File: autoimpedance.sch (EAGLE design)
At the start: 43 parts, among them IC1 AD5933, IC2 LM234, IC3 AD5245, Q1 DMG2307L-7

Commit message: Remove built for imp logo'
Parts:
- removed JP8: FIDUCIALUFIDUCIAL, SparkFun:FIDUCIALUFIDUCIAL
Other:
- note removed: "Electric Imp (based on their April design)"
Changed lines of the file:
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@@
 <part name="JP1" library="SparkFun-Connectors" deviceset="M02" device="SMD"/>
 <part name="U$5" library="SparkFun-Aesthetics" deviceset="OSHW-LOGO" device="S"/>
-<part name="JP8" library="SparkFun" deviceset="FIDUCIAL" device="UFIDUCIAL"/>
 <part name="OMNETICS" library="RHD2000" deviceset="OMNETICS_A79025" device=""/>
 <part name="IC1" library="autoimpedance" deviceset="AD5933" device=""/>
@@
 <text x="109.22" y="154.94" size="1.778" layer="97" rot="R90">1.5A</text>
 <text x="111.76" y="154.94" size="1.778" layer="97" rot="R90">VLF3014AT-2R2M1R2</text>
-<text x="150.622" y="6.35" size="3.048" layer="94">Electric Imp (based on their April design)</text>
 </plain>
 <instances>
@@
 <instance part="JP1" gate="G$1" x="10.16" y="119.38"/>
 <instance part="U$5" gate="G$1" x="132.08" y="10.16"/>
-<instance part="JP8" gate="G$1" x="243.84" y="33.02"/>
 <instance part="OMNETICS" gate="A" x="121.92" y="106.68" rot="R270"/>
 <instance part="IC1" gate="G$1" x="167.64" y="157.48"/>

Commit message: Fix incorrect VEE connection on 3x2 MUX
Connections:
- net 3.3V: no longer MUX3X2.VEE
- net GND: now also MUX3X2.VEE
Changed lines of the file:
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@@
 <part name="MUX3X2" library="open-ephys" deviceset="BU4053BC" device=""/>
 <part name="GND27" library="SparkFun-Aesthetics" deviceset="GND" device=""/>
-<part name="P+20" library="SparkFun-Aesthetics" deviceset="3.3V" device=""/>
 <part name="P+22" library="SparkFun-Aesthetics" deviceset="3.3V" device=""/>
 <part name="GND31" library="SparkFun-Aesthetics" deviceset="GND" device=""/>
@@
 <instance part="MUX3X2" gate="G$1" x="40.64" y="83.82"/>
 <instance part="GND27" gate="1" x="22.86" y="66.04"/>
-<instance part="P+20" gate="G$1" x="17.78" y="78.74"/>
 <instance part="P+22" gate="G$1" x="58.42" y="96.52"/>
 <instance part="GND31" gate="1" x="101.6" y="78.74"/>
@@
 <wire x1="30.48" y1="73.66" x2="22.86" y2="73.66" width="0.1524" layer="91"/>
 <wire x1="22.86" y1="73.66" x2="22.86" y2="68.58" width="0.1524" layer="91"/>
-<wire x1="22.86" y1="78.74" x2="22.86" y2="73.66" width="0.1524" layer="91"/>
+<wire x1="22.86" y1="78.74" x2="22.86" y2="76.2" width="0.1524" layer="91"/>
 <junction x="22.86" y="73.66"/>
 <pinref part="GND27" gate="1" pin="GND"/>
+<pinref part="MUX3X2" gate="G$1" pin="VEE"/>
+<wire x1="22.86" y1="76.2" x2="22.86" y2="73.66" width="0.1524" layer="91"/>
+<wire x1="30.48" y1="76.2" x2="22.86" y2="76.2" width="0.1524" layer="91"/>
+<junction x="22.86" y="76.2"/>
 </segment>
 <segment>
@@
 </segment>
 <segment>
-<pinref part="MUX3X2" gate="G$1" pin="VEE"/>
-<wire x1="30.48" y1="76.2" x2="17.78" y2="76.2" width="0.1524" layer="91"/>
-<wire x1="17.78" y1="76.2" x2="17.78" y2="78.74" width="0.1524" layer="91"/>
-<pinref part="P+20" gate="G$1" pin="3.3V"/>
-</segment>
-<segment>

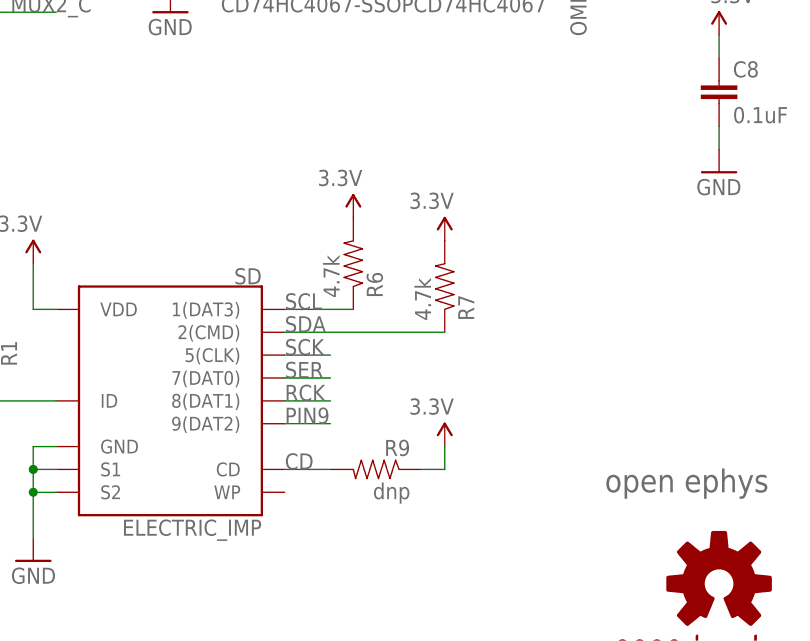
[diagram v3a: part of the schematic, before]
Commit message: Switch to i2c89 instead of i2c12
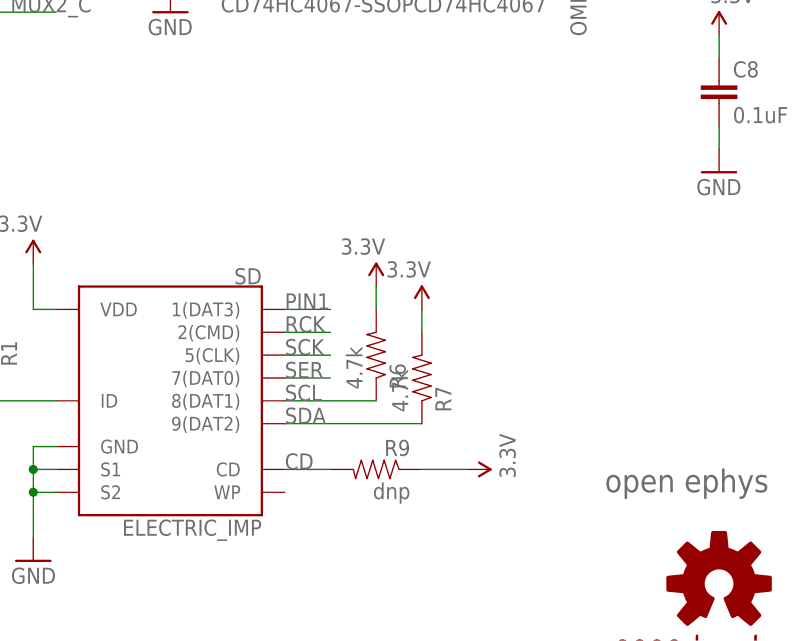
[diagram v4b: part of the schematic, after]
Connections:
- removed net PIN9: SD.9(DAT2)
- new net PIN1: SD.1(DAT3)
- net RCK: now also SD.2(CMD); no longer SD.8(DAT1)
- net SCL: now also SD.8(DAT1); no longer SD.1(DAT3)
- net SDA: now also SD.9(DAT2); no longer SD.2(CMD)
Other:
- moved on the sheet: R6, R7
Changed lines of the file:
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@@
 <instance part="GND13" gate="1" x="71.12" y="162.56"/>
 <instance part="GND14" gate="1" x="76.2" y="160.02"/>
-<instance part="R6" gate="G$1" x="91.44" y="45.72" rot="MR90"/>
-<instance part="R7" gate="G$1" x="101.6" y="43.18" rot="MR90"/>
-<instance part="P+6" gate="G$1" x="91.44" y="50.8" rot="MR0"/>
-<instance part="P+7" gate="G$1" x="101.6" y="48.26" rot="MR0"/>
+<instance part="R6" gate="G$1" x="93.98" y="35.56" rot="MR90"/>
+<instance part="R7" gate="G$1" x="99.06" y="33.02" rot="MR90"/>
+<instance part="P+6" gate="G$1" x="93.98" y="43.18" rot="MR0"/>
+<instance part="P+7" gate="G$1" x="99.06" y="40.64" rot="MR0"/>
 <instance part="P+8" gate="G$1" x="187.96" y="144.78" rot="R180"/>
 <instance part="GND15" gate="1" x="193.04" y="152.4"/>
@@
 <instance part="P+12" gate="G$1" x="238.76" y="162.56" rot="R270"/>
 <instance part="R9" gate="G$1" x="93.98" y="22.86" rot="MR0"/>
-<instance part="P+13" gate="G$1" x="101.6" y="25.4" rot="MR0"/>
+<instance part="P+13" gate="G$1" x="104.14" y="22.86" rot="MR90"/>
 <instance part="GND8" gate="1" x="152.4" y="53.34" rot="MR0"/>
 <instance part="GND20" gate="1" x="182.88" y="68.58" rot="MR270"/>
@@
 <pinref part="R6" gate="G$1" pin="2"/>
 <pinref part="P+6" gate="G$1" pin="3.3V"/>
+<wire x1="93.98" y1="40.64" x2="93.98" y2="43.18" width="0.1524" layer="91"/>
 </segment>
 <segment>
 <pinref part="R7" gate="G$1" pin="2"/>
 <pinref part="P+7" gate="G$1" pin="3.3V"/>
+<wire x1="99.06" y1="38.1" x2="99.06" y2="40.64" width="0.1524" layer="91"/>
 </segment>
 <segment>
@@
 <segment>
 <pinref part="R9" gate="G$1" pin="1"/>
-<wire x1="99.06" y1="22.86" x2="101.6" y2="22.86" width="0.1524" layer="91"/>
 <pinref part="P+13" gate="G$1" pin="3.3V"/>
-<wire x1="101.6" y1="22.86" x2="101.6" y2="25.4" width="0.1524" layer="91"/>
+<wire x1="99.06" y1="22.86" x2="104.14" y2="22.86" width="0.1524" layer="91"/>
 </segment>
 <segment>
@@
 </segment>
 </net>
-<net name="PIN9" class="0">
-<segment>
-<pinref part="SD" gate="G$1" pin="9(DAT2)"/>
-<wire x1="83.82" y1="27.94" x2="88.9" y2="27.94" width="0.1524" layer="91"/>
-<label x="83.82" y="27.94" size="1.778" layer="95"/>
-</segment>
-</net>
 <net name="CD" class="0">
 <segment>
@@
 <net name="SCL" class="0">
 <segment>
-<pinref part="SD" gate="G$1" pin="1(DAT3)"/>
-<label x="83.82" y="40.64" size="1.778" layer="95"/>
-<wire x1="83.82" y1="40.64" x2="91.44" y2="40.64" width="0.1524" layer="91"/>
-<pinref part="R6" gate="G$1" pin="1"/>
-</segment>
-<segment>
 <pinref part="IC1" gate="G$1" pin="SCL"/>
 <wire x1="182.88" y1="170.18" x2="193.04" y2="170.18" width="0.1524" layer="91"/>
@@
 <label x="182.88" y="106.68" size="1.778" layer="95"/>
 </segment>
+<segment>
+<pinref part="SD" gate="G$1" pin="8(DAT1)"/>
+<pinref part="R6" gate="G$1" pin="1"/>
+<wire x1="83.82" y1="30.48" x2="93.98" y2="30.48" width="0.1524" layer="91"/>
+<label x="83.82" y="30.48" size="1.778" layer="95"/>
+</segment>
 </net>
 <net name="SDA" class="0">
-<segment>
-<pinref part="SD" gate="G$1" pin="2(CMD)"/>
-<label x="83.82" y="38.1" size="1.778" layer="95"/>
-<wire x1="83.82" y1="38.1" x2="101.6" y2="38.1" width="0.1524" layer="91"/>
-<pinref part="R7" gate="G$1" pin="1"/>
-</segment>
 <segment>
 <pinref part="IC1" gate="G$1" pin="SDA"/>
@@
 <wire x1="190.5" y1="109.22" x2="182.88" y2="109.22" width="0.1524" layer="91"/>
 <label x="182.88" y="109.22" size="1.778" layer="95"/>
+</segment>
+<segment>
+<pinref part="SD" gate="G$1" pin="9(DAT2)"/>
+<pinref part="R7" gate="G$1" pin="1"/>
+<wire x1="83.82" y1="27.94" x2="99.06" y2="27.94" width="0.1524" layer="91"/>
+<label x="83.82" y="27.94" size="1.778" layer="95"/>
 </segment>
 </net>
@@
 </segment>
 <segment>
-<pinref part="SD" gate="G$1" pin="8(DAT1)"/>
-<wire x1="83.82" y1="30.48" x2="88.9" y2="30.48" width="0.1524" layer="91"/>
-<label x="83.82" y="30.48" size="1.778" layer="95"/>
+<pinref part="SD" gate="G$1" pin="2(CMD)"/>
+<wire x1="83.82" y1="38.1" x2="88.9" y2="38.1" width="0.1524" layer="91"/>
+<label x="83.82" y="38.1" size="1.778" layer="95"/>
 </segment>
 </net>
@@
 </segment>
 </net>
+<net name="PIN1" class="0">
+<segment>
+<pinref part="SD" gate="G$1" pin="1(DAT3)"/>
+<wire x1="83.82" y1="40.64" x2="88.9" y2="40.64" width="0.1524" layer="91"/>
+<label x="83.82" y="40.64" size="1.778" layer="95"/>
+</segment>
+</net>
